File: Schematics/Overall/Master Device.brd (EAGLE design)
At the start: 50 x 70 mm, 40 parts, among them J1 POWER_JACK, U1 MPU-6050-1

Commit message: eagle cad is cancer
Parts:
- moved MPU_BO 103.6 mm to (47.1, 2.30), turned to 180 degrees
- moved HC-05 78.3 mm to (32.4, 40.0)
- moved SJ2 53.4 mm to (12.8, 16.0), turned to 90 degrees
- moved SDCARD_READER 52.2 mm to (18.8, 33.5), turned to 270 degrees
- moved C2 38.4 mm to (6.02, 20.1), turned to 180 degrees
- moved C5 35.4 mm to (19.4, 41.8), turned to 270 degrees
- moved MICROCONTROLLER 27.0 mm to (6.67, 49.0)
- moved R11 23.9 mm to (21.0, 48.4), turned to 90 degrees
- moved C4 20.2 mm to (19.3, 59.8), turned to 270 degrees
- moved FSR2 19.7 mm to (16.7, 52.0), turned to 270 degrees
- moved R8 17.6 mm to (20.9, 53.0)
- moved R7 14.0 mm to (20.8, 74.7)
- moved R6 13.6 mm to (15.3, 74.7), turned to 0 degrees
- moved RESET 13.2 mm to (11.8, 80.4)
- moved D1 13.0 mm to (2.86, 78.5)
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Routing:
- net GND: track 39.7 -> 0.00 mm
- net N$7: track 0.00 -> 5.02 mm
- net N$6: track 0.00 -> 3.42 mm
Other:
- board size 50 x 70 mm -> 50 x 87 mm
- board text added: "Bluetooth module"
- board text added: "MPU Brkout"
- board text added: "SD Reader"

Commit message: WIP
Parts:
- moved R13 111.9 mm to (43.6, 3.96), turned to 180 degrees
- moved C8 105.6 mm to (46.2, 8.64), turned to 90 degrees
- moved R12 103.7 mm to (37.9, 3.89)
- moved C9 94.2 mm to (32.5, 14.4), turned to 180 degrees
- moved C7 93.3 mm to (34.1, 5.55), turned to 90 degrees
- moved C6 89.9 mm to (39.6, 15.4)
- moved SJ3 80.5 mm to (45.8, 12.8), turned to 180 degrees
- moved U1 80.0 mm to (39.0, 9.55), turned to 180 degrees
- moved C3 66.6 mm to (19.0, 19.5), turned to 90 degrees
- moved R9 66.5 mm to (18.6, 24.9)
- moved C1 57.3 mm to (15.1, 19.5), turned to 90 degrees
- moved R5 50.9 mm to (14.4, 25.0)
- moved FRAME1 45.2 mm to (5.68, 25.2)
- moved R4 45.1 mm to (9.60, 24.9), turned to 180 degrees
- moved C2 41.9 mm to (33.0, 52.1)
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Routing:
- net GND: track 0.00 -> 301.2 mm, vias 0 -> 5
- net +3V3: track 0.00 -> 146.8 mm, vias 0 -> 3
- net 9V_BAT: track 0.00 -> 39.3 mm, vias 0 -> 1
- net CLKIN: track 0.00 -> 15.2 mm, vias 0 -> 2
- net N$2: track 0.00 -> 7.72 mm
- net N$14: track 0.00 -> 7.26 mm
- net N$8: track 0.00 -> 7.10 mm
- net SDA: track 0.00 -> 6.99 mm
- net N$12: track 0.00 -> 6.89 mm
- net N$3: track 0.00 -> 6.41 mm
- net N$11: track 0.00 -> 6.36 mm
- net N$9: track 0.00 -> 5.55 mm
- net SCL: track 0.00 -> 4.98 mm
- net FSR1: track 0.00 -> 3.75 mm
- net N$10: track 0.00 -> 3.73 mm
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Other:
- board size 50 x 87 mm -> 50 x 90 mm

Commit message: Finished this fucking piece of shit
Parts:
- moved J1 3.16 mm to (7.96, 14.0)
- moved C7 2.24 mm to (33.1, 7.55)
- moved C9 2.24 mm to (30.5, 13.4)
- moved SJ2 2.24 mm to (30.0, 10.2)
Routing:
- net SDA: track 6.99 -> 122.8 mm, vias 0 -> 6
- net MPU_INT: track 0.00 -> 108.6 mm, vias 0 -> 3
- net TXA: track 0.00 -> 98.9 mm, vias 0 -> 3
- net +3V3: track 146.8 -> 245.6 mm, vias 3 -> 7
- net SCL: track 4.98 -> 100.9 mm, vias 0 -> 4
- net RXA: track 0.00 -> 88.5 mm, vias 0 -> 3
- net GND: track 301.2 -> 370.8 mm
- net N$4: track 0.00 -> 54.6 mm
- net N$5: track 0.00 -> 53.9 mm
- net V_MON: track 3.34 -> 56.9 mm, vias 0 -> 1
- net SENSE: track 2.46 -> 43.2 mm, vias 0 -> 2
- net FSR2: track 3.61 -> 39.2 mm, vias 0 -> 1
- net SPI_MISO: track 0.00 -> 33.5 mm, vias 0 -> 1
- net N$2: track 7.72 -> 40.8 mm
- net SPI_SCLK: track 0.00 -> 31.5 mm
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
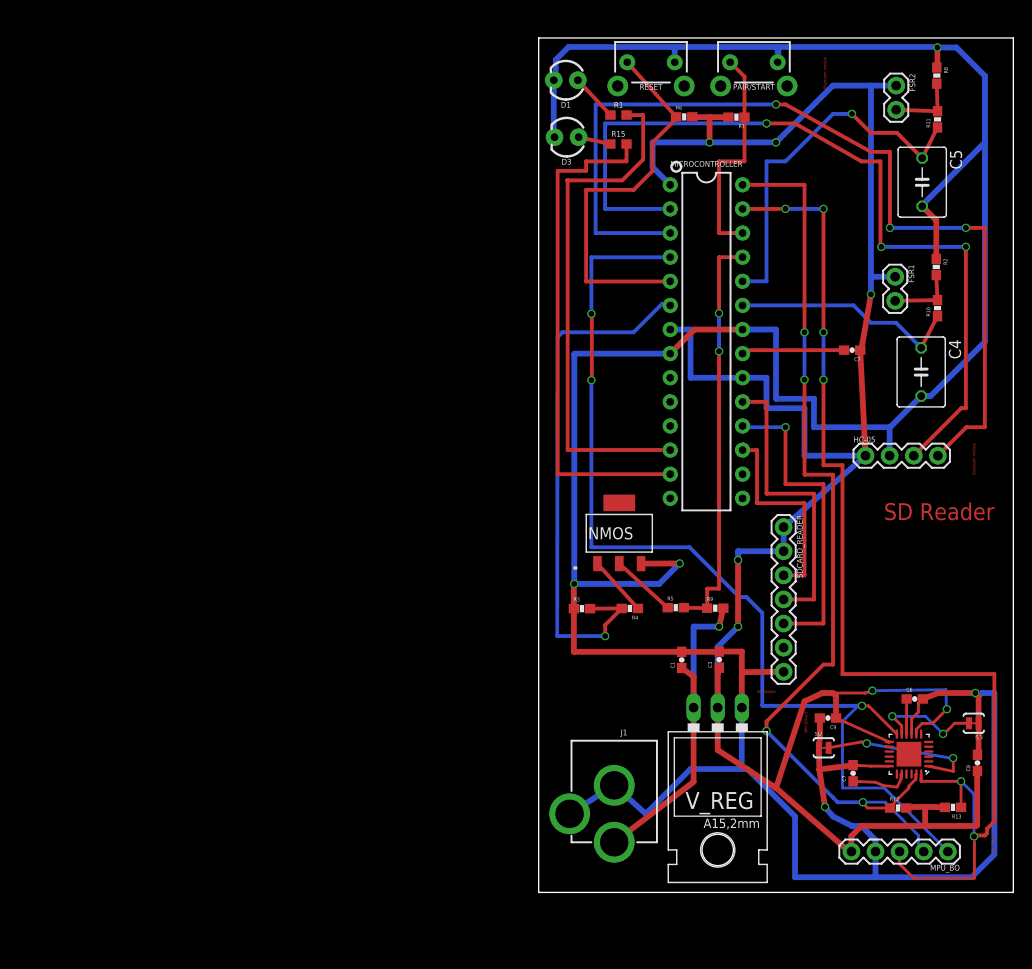
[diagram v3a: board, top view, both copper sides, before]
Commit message: Added shape node to bottom for GND
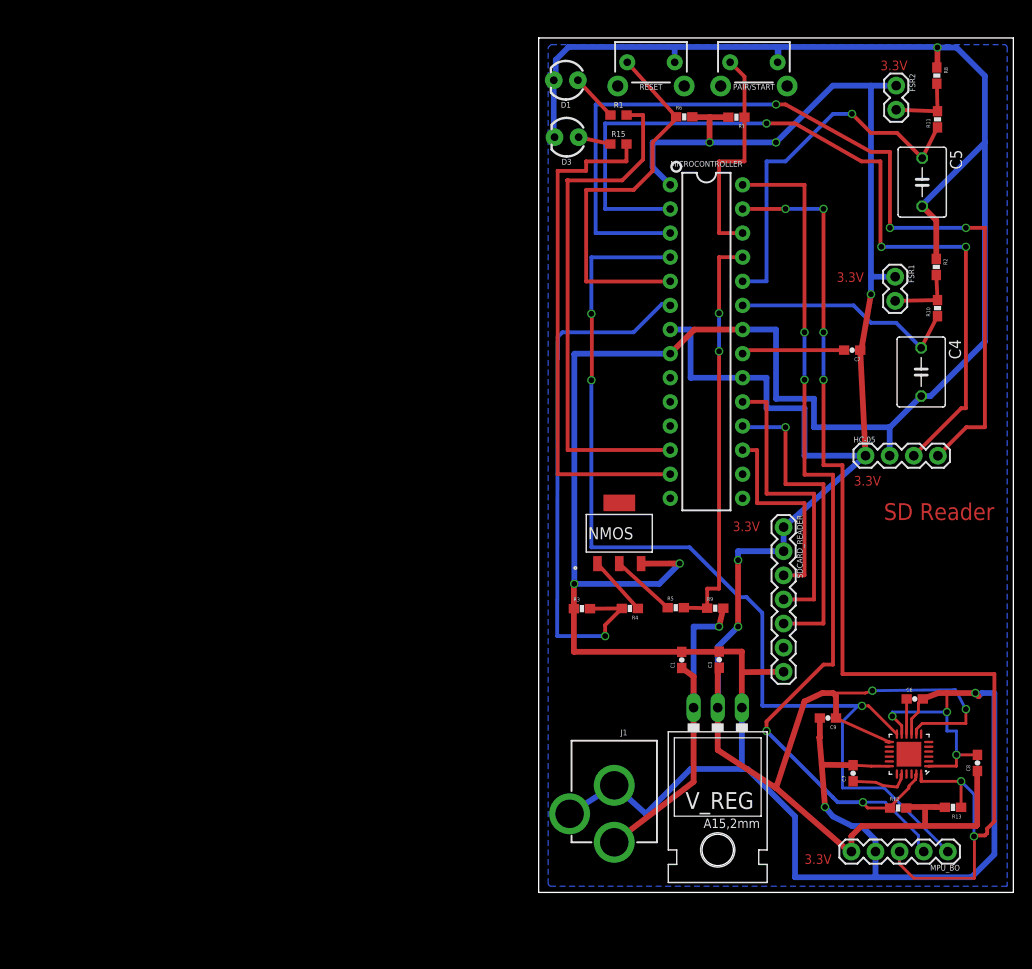
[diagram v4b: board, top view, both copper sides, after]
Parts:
- removed SJ2, SJ3: (no value), SparkFun:SJ_2S-TRACE
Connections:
- removed net CLKIN: SJ2.2, U1.1
- removed net FSYNC: SJ3.2, U1.11
- net GND: now also U1.1, U1.11; no longer SJ2.1, SJ3.1
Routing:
- net CLKIN: track 17.4 -> 0.00 mm, vias 2 -> 0
- net GND: track 370.8 -> 386.9 mm, vias 5 -> 8
- net FSYNC: track 11.6 -> 0.00 mm, vias 2 -> 0
- net +3V3: track 245.6 -> 249.8 mm
- added copper zone on layer 16, net GND
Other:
- board text added: "3.3V"
- board text removed: "Bluetooth module"
- board text removed: "MPU Brkout"
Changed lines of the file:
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@@
 <drawing>
 <settings>
-<setting alwaysvectorfont="no"/>
+<setting alwaysvectorfont="yes"/>
 <setting verticaltext="up"/>
 </settings>
@@
 <wire x1="50" y1="85" x2="0" y2="85" width="0" layer="20"/>
 <wire x1="0" y1="85" x2="0" y2="-5" width="0" layer="20"/>
-<text x="46" y="39" size="0.3048" layer="1" rot="R90">Bluetooth module</text>
-<text x="23" y="16" size="0.3048" layer="1">SD Reader</text>
-<text x="28" y="14" size="0.3048" layer="1" rot="R270">MPU Brkout</text>
-<text x="48" y="36" size="1.778" layer="1" rot="R180">SD Reader</text>
-<text x="30" y="83" size="0.3048" layer="1" rot="R270">Bluetooth module</text>
-<text x="48" y="-1" size="0.3048" layer="1" rot="R90">MPU Brkout</text>
+<text x="48" y="36" size="1.778" layer="1" ratio="16" rot="R180">SD Reader</text>
+<text x="28" y="-2" size="1.016" layer="1" ratio="16">3.3V</text>
+<text x="20.45" y="33.05" size="1.016" layer="1" ratio="16">3.3V</text>
+<text x="36" y="81.6" size="1.016" layer="1" ratio="16">3.3V</text>
+<text x="31.4" y="59.3" size="1.016" layer="1" ratio="16">3.3V</text>
+<text x="33.2" y="37.85" size="1.016" layer="1" ratio="16">3.3V</text>
 </plain>
 <attributes>
@@
 </element>
 <element name="SDCARD_READER" library="SparkFun-Connectors" package="1X07" value="SD_READER" x="25.8" y="33.48" rot="R270"/>
-<element name="SJ2" library="SparkFun" package="SJ_2S-TRACE" value="" x="30.03" y="10.23"/>
-<element name="SJ3" library="SparkFun" package="SJ_2S-TRACE" value="" x="45.83" y="12.82" rot="R180"/>
 <element name="U1" library="Testing" package="QFN-24-4MM2" value="MPU-6050-1" x="39.02" y="9.55" rot="R180"/>
 <element name="V_REG" library="SparkFun-IC-Power" package="78XXL" value="LD1117V33" x="18.86" y="10.65" rot="R180"/>
@@
 <contactref element="C8" pad="2"/>
 <contactref element="U1" pad="18"/>
-<contactref element="SJ2" pad="1"/>
-<contactref element="SJ3" pad="1"/>
 <contactref element="U1" pad="9"/>
 <contactref element="NMOS" pad="3"/>
@@
 <wire x1="31" y1="3" x2="30.16285625" y2="4" width="0.6096" layer="16"/>
 <via x="30.16285625" y="4" extent="1-16" drill="0.6" shape="square"/>
-<wire x1="29.56285625" y1="7.95" x2="30.16285625" y2="4" width="0.6096" layer="1"/>
-<wire x1="29.56285625" y1="7.95" x2="33.12" y2="8.4" width="0.6096" layer="1"/>
-<wire x1="29.56285625" y1="7.95" x2="29.522" y2="10.23" width="0.6096" layer="1"/>
+<wire x1="29.81285625" y1="8.45" x2="30.16285625" y2="4" width="0.6096" layer="1"/>
+<wire x1="29.81285625" y1="8.45" x2="33.12" y2="8.4" width="0.6096" layer="1"/>
 <wire x1="21.4" y1="18.2" x2="21.4" y2="14.46" width="0.6096" layer="1"/>
 <wire x1="21.4" y1="18.2" x2="21.4" y2="20.37" width="0.6096" layer="1"/>
@@
 <wire x1="36.97" y1="43.96" x2="36.97" y2="41" width="0.6096" layer="16"/>
 <wire x1="42.08" y1="16" x2="40.46" y2="15.38" width="0.6096" layer="1"/>
-<wire x1="46" y1="16" x2="42.08" y2="16" width="0.6096" layer="1"/>
-<wire x1="46.338" y1="15.662" x2="46.338" y2="12.82" width="0.6096" layer="1"/>
+<wire x1="43" y1="16" x2="46" y2="16" width="0.6096" layer="1"/>
+<wire x1="43" y1="16" x2="42.08" y2="16" width="0.6096" layer="1"/>
 <wire x1="46.338" y1="15.662" x2="46" y2="16" width="0.6096" layer="1"/>
-<wire x1="46.338" y1="12.82" x2="46.338" y2="9.608" width="0.6096" layer="1"/>
-<wire x1="46.338" y1="9.608" x2="46.22" y2="9.49" width="0.6096" layer="1"/>
+<wire x1="46.22" y1="9.49" x2="46.338" y2="9.608" width="0.6096" layer="1"/>
 <wire x1="35.48" y1="-3.4" x2="45.6" y2="-3.4" width="0.6096" layer="16"/>
 <wire x1="45.6" y1="-3.4" x2="48" y2="-1" width="0.6096" layer="16"/>
@@
 <wire x1="40" y1="14" x2="39.2775" y2="13.2775" width="0.3048" layer="1"/>
 <wire x1="39.2775" y1="13.2775" x2="39.2775" y2="11.6716" width="0.3048" layer="1"/>
-<wire x1="29.522" y1="10.23" x2="29.62" y2="11.328" width="0.6096" layer="1"/>
-<wire x1="29.62" y1="11.328" x2="29.62" y2="13.37" width="0.6096" layer="1"/>
+<wire x1="29.62" y1="13.37" x2="29.62" y2="11.328" width="0.6096" layer="1"/>
 <wire x1="3.75" y1="27.5" x2="3.75" y2="51.7" width="0.6096" layer="16"/>
 <wire x1="3.75" y1="51.7" x2="3.8" y2="51.75" width="0.6096" layer="16"/>
@@
 <wire x1="25" y1="54.29" x2="21.48" y2="54.29" width="0.6096" layer="16"/>
 <wire x1="36.93" y1="44" x2="29" y2="44" width="0.6096" layer="16"/>
+<contactref element="U1" pad="11"/>
+<via x="37.25" y="13.55" extent="1-16" drill="0.6" shape="square"/>
+<wire x1="37.25" y1="13.55" x2="38.2404" y2="12.5596" width="0.3048" layer="1"/>
+<wire x1="38.2404" y1="12.5596" x2="38.2404" y2="11.6716" width="0.3048" layer="1"/>
+<contactref element="U1" pad="1"/>
+<wire x1="29.62" y1="11.328" x2="29.56285625" y2="11.328" width="0.6096" layer="1"/>
+<wire x1="29.56285625" y1="11.328" x2="29.81285625" y2="8.45" width="0.6096" layer="1"/>
+<wire x1="41.0862" y1="8.2933" x2="41.0862" y2="8.3" width="0.3048" layer="1"/>
+<wire x1="41.0862" y1="8.3" x2="44" y2="8.3" width="0.3048" layer="1"/>
+<wire x1="44" y1="9.49" x2="46.22" y2="9.49" width="0.3048" layer="1"/>
+<via x="44" y="9.49" extent="1-16" drill="0.6" shape="square"/>
+<wire x1="44" y1="8.3" x2="44" y2="9.49" width="0.3048" layer="1"/>
+<wire x1="44" y1="9.49" x2="44" y2="12" width="0.3048" layer="16"/>
+<wire x1="44" y1="12" x2="43" y2="12" width="0.3048" layer="16"/>
+<wire x1="43" y1="14" x2="43" y2="12" width="0.3048" layer="16"/>
+<via x="43" y="14" extent="1-16" drill="0.6" shape="square"/>
+<wire x1="43" y1="14" x2="43" y2="16" width="0.3048" layer="1"/>
+<wire x1="37.25" y1="13.55" x2="37.25" y2="14" width="0.3048" layer="16"/>
+<wire x1="37.25" y1="14" x2="43" y2="14" width="0.3048" layer="16"/>
+<polygon width="0.3048" layer="16" isolate="1.27">
+<vertex x="1" y="84"/>
+<vertex x="1.3" y="84.3"/>
+<vertex x="49.15" y="84.3"/>
+<vertex x="49.35" y="84.1"/>
+<vertex x="49.35" y="-4.35"/>
+<vertex x="1.2" y="-4.35"/>
+<vertex x="1" y="-4.15"/>
+</polygon>
 </signal>
 <signal name="N$1">
@@
 <wire x1="32.7" y1="-0.7" x2="25" y2="6" width="0.6096" layer="1"/>
 <via x="35.15" y="16.25" extent="1-16" drill="0.6" shape="square"/>
-<wire x1="35.15" y1="16.25" x2="42.9" y2="16.35" width="0.3048" layer="16"/>
-<wire x1="42.9" y1="16.35" x2="42.95" y2="14.35" width="0.3048" layer="16"/>
-<wire x1="42.95" y1="14.35" x2="43" y2="14.3" width="0.3048" layer="16"/>
-<via x="43" y="14.3" extent="1-16" drill="0.6" shape="square"/>
+<wire x1="35.15" y1="16.25" x2="43.9" y2="16.35" width="0.3048" layer="16"/>
+<wire x1="43.9" y1="16.35" x2="44.95" y2="14.35" width="0.3048" layer="16"/>
+<wire x1="44.95" y1="14.35" x2="45" y2="14.3" width="0.3048" layer="16"/>
+<via x="45" y="14.3" extent="1-16" drill="0.6" shape="square"/>
 <wire x1="39.7821" y1="11.6716" x2="39.7821" y2="12.1821" width="0.3048" layer="1"/>
 <wire x1="39.7821" y1="12.1821" x2="40.4" y2="12.8" width="0.3048" layer="1"/>
-<wire x1="40.4" y1="12.8" x2="41.5" y2="12.8" width="0.3048" layer="1"/>
-<wire x1="41.5" y1="12.8" x2="43" y2="14.3" width="0.3048" layer="1"/>
+<wire x1="40.4" y1="12.8" x2="45" y2="12.8" width="0.3048" layer="1"/>
+<wire x1="45" y1="12.8" x2="45" y2="14.3" width="0.3048" layer="1"/>
 <wire x1="35.15" y1="16.25" x2="34.4" y2="16" width="0.3048" layer="1"/>
 <wire x1="34.4" y1="16" x2="31" y2="16" width="0.3048" layer="1"/>
@@
 <wire x1="13.86" y1="61.91" x2="13.86" y2="61.91" width="0" layer="19" extent="1-16"/>
 </signal>
-<signal name="FSYNC">
-<contactref element="U1" pad="11"/>
-<contactref element="SJ3" pad="2"/>
-<wire x1="45.322" y1="12.82" x2="43.82" y2="12.82" width="0.3048" layer="1"/>
-<wire x1="43.82" y1="12.82" x2="42.7" y2="11.7" width="0.3048" layer="1"/>
-<wire x1="42.7" y1="11.7" x2="42.6" y2="11.7" width="0.3048" layer="1"/>
-<via x="42.6" y="11.7" extent="1-16" drill="0.6" shape="square"/>
-<wire x1="42.6" y1="11.7" x2="40.75" y2="13.55" width="0.3048" layer="16"/>
-<via x="37.25" y="13.55" extent="1-16" drill="0.6" shape="square"/>
-<wire x1="37.25" y1="13.55" x2="38.2404" y2="12.5596" width="0.3048" layer="1"/>
-<wire x1="38.2404" y1="12.5596" x2="38.2404" y2="11.6716" width="0.3048" layer="1"/>
-<wire x1="40.75" y1="13.55" x2="37.25" y2="13.55" width="0.3048" layer="16"/>
-</signal>
-<signal name="CLKIN">
-<contactref element="U1" pad="1"/>
-<contactref element="SJ2" pad="2"/>
-<wire x1="30.538" y1="10.23" x2="34" y2="10.85" width="0.3048" layer="1"/>
-<wire x1="34" y1="10.85" x2="34.55" y2="10.7" width="0.3048" layer="1"/>
-<via x="34.55" y="10.7" extent="1-16" drill="0.6" shape="square"/>
-<wire x1="34.55" y1="10.7" x2="43.65" y2="9.1" width="0.3048" layer="16"/>
-<wire x1="43.65" y1="9.1" x2="43.65" y2="9.15" width="0.3048" layer="16"/>
-<via x="43.65" y="9.15" extent="1-16" drill="0.6" shape="square"/>
-<wire x1="43.65" y1="9.15" x2="43.7" y2="7.75" width="0.3048" layer="1"/>
-<wire x1="43.7" y1="7.75" x2="41.0862" y2="8.2933" width="0.3048" layer="1"/>
-</signal>
 <signal name="SENSE">
